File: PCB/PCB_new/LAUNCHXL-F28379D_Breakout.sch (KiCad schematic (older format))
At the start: 21 parts, among them IC1 LM358N, J10 SERVO_CONN, J11 MC_CONN, Q1 220mA/50V/3.5Ω, Q2 100V/17A, Q3 100V/17A, Q4 100V/17A, Q5 100V/17A, Q6 100V/17A

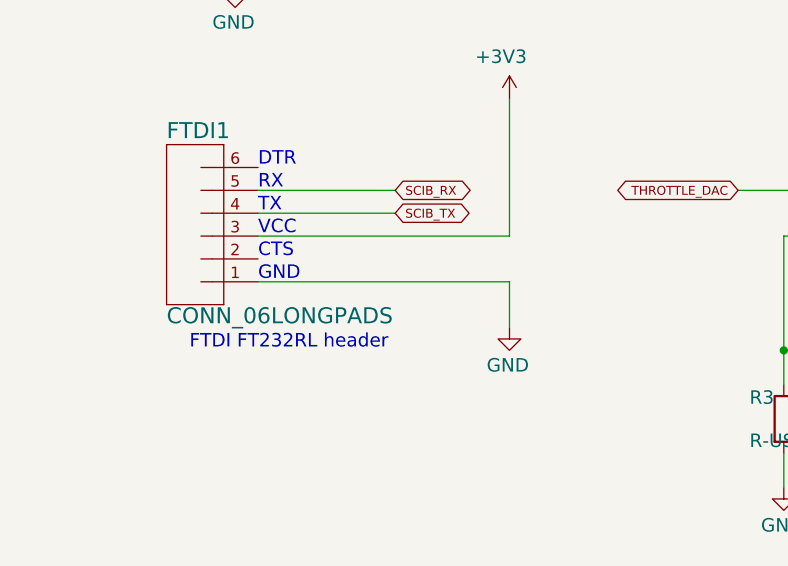
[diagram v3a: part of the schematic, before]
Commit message: changed components footprints to Drivetrain.pretty
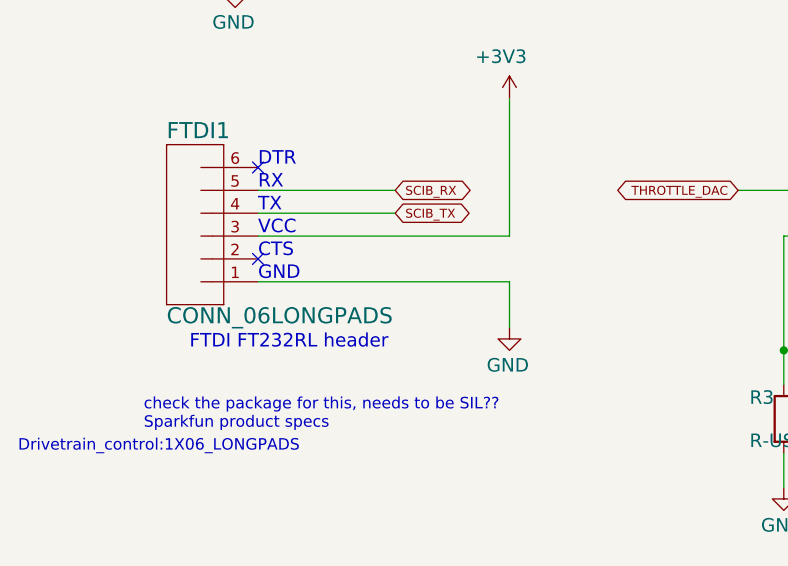
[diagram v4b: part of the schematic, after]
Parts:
- C1: footprint Drivetrain_control:C0805 -> Capacitor_SMD:C_0805_2012Metric_Pad1.15x1.40mm_HandSolder
- DCDC_CONN_12V: footprint Connector_Molex:Molex_CLIK-Mate_502382-0270_1x02-1MP_P1.25mm_Vertical -> Drivetrain_control:22-23-2021
- IC1: footprint Package_DIP:DIP-8_W10.16mm -> Drivetrain_control:DIL08
- J10: footprint (none) -> Drivetrain_control:5566-8
- JETSON_CONN_PWR: footprint Connector_Molex:Molex_CLIK-Mate_502382-0370_1x03-1MP_P1.25mm_Vertical -> Drivetrain_control:22-23-2031
- Q1: footprint Package_TO_SOT_THT:TO-251-3_Vertical -> Drivetrain_control:SOT23-3
- Q2, Q3, Q4, Q5, Q6: footprint Package_TO_SOT_THT:TO-251-3_Vertical -> Drivetrain_control:TO220V
- R1, R18, R2, R3, R4, R5: footprint Drivetrain_control:R0805 -> Resistor_SMD:R_0805_2012Metric_Pad1.15x1.40mm_HandSolder
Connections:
- no-connect marks 0 -> 2
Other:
- note added: "Drivetrain_control:1X06_LONGPADS"
- note added: "check the package for this, needs to be SIL??\nSparkfun product specs"
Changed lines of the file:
@@
 F 0 "R4" V 4600 4200 59  0000 L BNN
 F 1 "R-US_R0805" V 4600 3550 59  0000 L BNN
-F 2 "Drivetrain_control:R0805" H 4700 4100 50  0001 C CNN
+F 2 "Resistor_SMD:R_0805_2012Metric_Pad1.15x1.40mm_HandSolder" H 4700 4100 50  0001 C CNN
 F 3 "" H 4700 4100 50  0001 C CNN
 	1    4700 4100
@@
 F 0 "IC1" H 4750 3625 59  0001 L BNN
 F 1 "LM358N" H 4750 3300 59  0001 L BNN
-F 2 "Package_DIP:DIP-8_W10.16mm" H 4650 3500 50  0001 C CNN
+F 2 "Drivetrain_control:DIL08" H 4650 3500 50  0001 C CNN
 F 3 "" H 4650 3500 50  0001 C CNN
 	1    4650 3500
@@
 F 0 "C1" H 5360 3115 59  0000 L BNN
 F 1 "0.1uF" H 5360 2915 59  0000 L BNN
-F 2 "Drivetrain_control:C0805" H 5300 3100 50  0001 C CNN
+F 2 "Capacitor_SMD:C_0805_2012Metric_Pad1.15x1.40mm_HandSolder" H 5300 3100 50  0001 C CNN
 F 3 "" H 5300 3100 50  0001 C CNN
 	1    5300 3100
@@
 F 0 "Q1" V 5600 1550 70  0000 L BNN
 F 1 "220mA/50V/3.5Ω" V 5700 1350 70  0000 L BNN
-F 2 "Package_TO_SOT_THT:TO-251-3_Vertical" H 5300 1600 50  0001 C CNN
+F 2 "Drivetrain_control:SOT23-3" H 5300 1600 50  0001 C CNN
 F 3 "" H 5300 1600 50  0001 C CNN
 	1    5300 1600
@@
 F 0 "R1" H 4600 1550 59  0000 L BNN
 F 1 "10k" H 4550 1450 59  0000 L BNN
-F 2 "Drivetrain_control:R0805" H 4800 1500 50  0001 C CNN
+F 2 "Resistor_SMD:R_0805_2012Metric_Pad1.15x1.40mm_HandSolder" H 4800 1500 50  0001 C CNN
 F 3 "" H 4800 1500 50  0001 C CNN
 	1    4800 1500
@@
 F 0 "R5" H 6550 2759 59  0000 L BNN
 F 1 "R-US_R0805" H 6550 2570 59  0000 L BNN
-F 2 "Drivetrain_control:R0805" H 6700 2700 50  0001 C CNN
+F 2 "Resistor_SMD:R_0805_2012Metric_Pad1.15x1.40mm_HandSolder" H 6700 2700 50  0001 C CNN
 F 3 "" H 6700 2700 50  0001 C CNN
 	1    6700 2700
@@
 F 0 "Q2" H 7900 3200 70  0000 L BNN
 F 1 "100V/17A" H 7900 3100 70  0000 L BNN
-F 2 "Package_TO_SOT_THT:TO-251-3_Vertical" H 7700 3200 50  0001 C CNN
+F 2 "Drivetrain_control:TO220V" H 7700 3200 50  0001 C CNN
 F 3 "" H 7700 3200 50  0001 C CNN
 	1    7700 3200
@@
 F 0 "R18" H 7650 2759 59  0000 L BNN
 F 1 "R-US_R0805" H 7650 2570 59  0000 L BNN
-F 2 "Drivetrain_control:R0805" H 7800 2700 50  0001 C CNN
+F 2 "Resistor_SMD:R_0805_2012Metric_Pad1.15x1.40mm_HandSolder" H 7800 2700 50  0001 C CNN
 F 3 "" H 7800 2700 50  0001 C CNN
 	1    7800 2700
@@
 F 0 "JETSON_CONN_PWR1" H 9800 1400 51  0000 L BNN
 F 1 "22-23-2031" H 10470 1655 59  0001 L BNN
-F 2 "Connector_Molex:Molex_CLIK-Mate_502382-0370_1x03-1MP_P1.25mm_Vertical" H 10500 1600 50  0001 C CNN
+F 2 "Drivetrain_control:22-23-2031" H 10500 1600 50  0001 C CNN
 F 3 "" H 10500 1600 50  0001 C CNN
 	1    10500 1600
@@
 F 0 "Q3" H 6800 3200 70  0000 L BNN
 F 1 "100V/17A" H 6800 3100 70  0000 L BNN
-F 2 "Package_TO_SOT_THT:TO-251-3_Vertical" H 6600 3200 50  0001 C CNN
+F 2 "Drivetrain_control:TO220V" H 6600 3200 50  0001 C CNN
 F 3 "" H 6600 3200 50  0001 C CNN
 	1    6600 3200
@@
 F 0 "Q4" H 9000 3200 70  0000 L BNN
 F 1 "100V/17A" H 9000 3100 70  0000 L BNN
-F 2 "Package_TO_SOT_THT:TO-251-3_Vertical" H 8800 3200 50  0001 C CNN
+F 2 "Drivetrain_control:TO220V" H 8800 3200 50  0001 C CNN
 F 3 "" H 8800 3200 50  0001 C CNN
 	1    8800 3200
@@
 F 0 "Q5" H 10100 3200 70  0000 L BNN
 F 1 "100V/17A" H 10100 3100 70  0000 L BNN
-F 2 "Package_TO_SOT_THT:TO-251-3_Vertical" H 9900 3200 50  0001 C CNN
+F 2 "Drivetrain_control:TO220V" H 9900 3200 50  0001 C CNN
 F 3 "" H 9900 3200 50  0001 C CNN
 	1    9900 3200
@@
 F 0 "Q6" H 11200 3200 70  0000 L BNN
 F 1 "100V/17A" H 11200 3100 70  0000 L BNN
-F 2 "Package_TO_SOT_THT:TO-251-3_Vertical" H 11000 3200 50  0001 C CNN
+F 2 "Drivetrain_control:TO220V" H 11000 3200 50  0001 C CNN
 F 3 "" H 11000 3200 50  0001 C CNN
 	1    11000 3200
@@
 F 0 "R3" H 4150 4459 59  0000 L BNN
 F 1 "R-US_R0805" H 4150 4270 59  0000 L BNN
-F 2 "Drivetrain_control:R0805" H 4300 4400 50  0001 C CNN
+F 2 "Resistor_SMD:R_0805_2012Metric_Pad1.15x1.40mm_HandSolder" H 4300 4400 50  0001 C CNN
 F 3 "" H 4300 4400 50  0001 C CNN
 	1    4300 4400
@@
 F 0 "R2" H 5600 1500 59  0000 L BNN
 F 1 "10k" H 5550 1400 59  0000 L BNN
-F 2 "Drivetrain_control:R0805" H 5800 1500 50  0001 C CNN
+F 2 "Resistor_SMD:R_0805_2012Metric_Pad1.15x1.40mm_HandSolder" H 5800 1500 50  0001 C CNN
 F 3 "" H 5800 1500 50  0001 C CNN
 	1    5800 1500
@@
 F 0 "DCDC_CONN_12V1" H 6900 1450 51  0000 L BNN
 F 1 "22-23-2021" H 7570 1555 59  0001 L BNN
-F 2 "Connector_Molex:Molex_CLIK-Mate_502382-0270_1x02-1MP_P1.25mm_Vertical" H 7600 1500 50  0001 C CNN
+F 2 "Drivetrain_control:22-23-2021" H 7600 1500 50  0001 C CNN
 F 3 "" H 7600 1500 50  0001 C CNN
 	1    7600 1500
@@
 F 0 "J10" H 3172 1382 50  0000 R CNN
 F 1 "SERVO_CONN" H 3172 1473 50  0000 R CNN
-F 2 "" H 3200 1500 50  0001 C CNN
+F 2 "Drivetrain_control:5566-8" H 3200 1500 50  0001 C CNN
 F 3 "~" H 3200 1500 50  0001 C CNN
 	1    3200 1500
@@
 Wire Wire Line
 	2650 1800 2650 2100
+NoConn ~ 2000 3300
+NoConn ~ 2000 3700
+Text Notes 950  4550 0    50   ~ 0
+Drivetrain_control:1X06_LONGPADS
+Text Notes 1500 4450 0    50   ~ 0
+check the package for this, needs to be SIL??\nSparkfun product specs
 $EndSCHEMATC

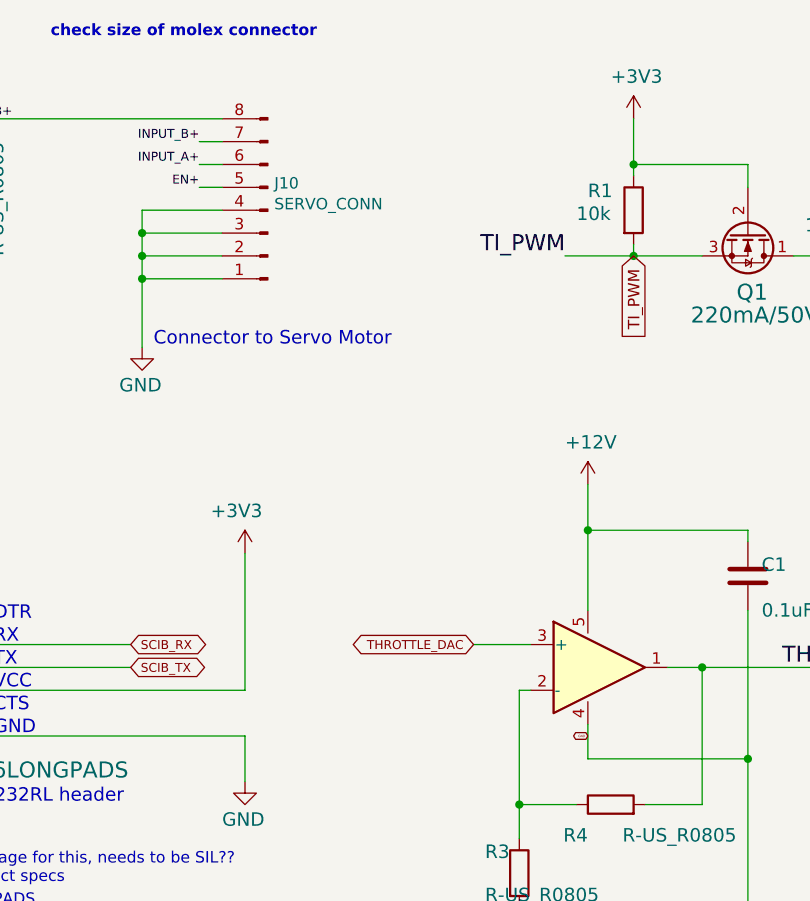
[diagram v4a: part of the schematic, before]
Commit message: tried to update PCB with new components but got weird results (not working)
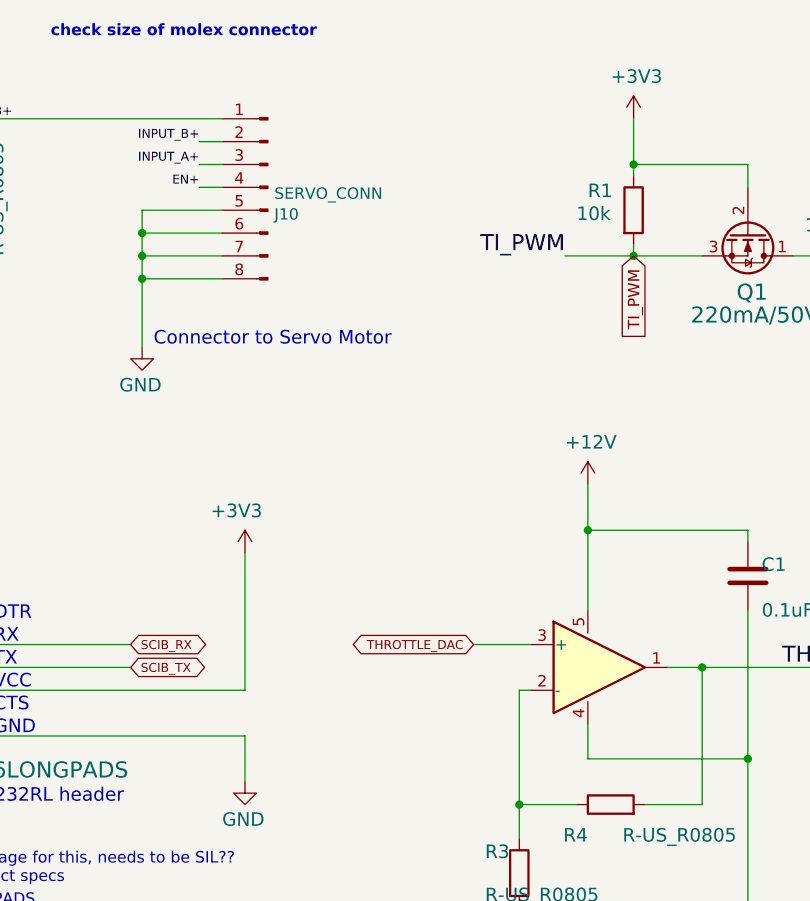
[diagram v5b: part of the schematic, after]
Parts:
- J11: footprint Connector_Molex:Molex_Mini-Fit_Jr_5566-04A2_2x02_P4.20mm_Vertical -> Drivetrain_control:22-23-2041
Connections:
- net EN+: now also J10.4 (Pin_4); no longer J10.5 (Pin_5)
- net GND: now also J10.5 (Pin_5), J10.6 (Pin_6), J10.7 (Pin_7), J10.8 (Pin_8); no longer J10.1 (Pin_1), J10.2 (Pin_2), J10.3 (Pin_3), J10.4 (Pin_4)
- net HLFB+: now also J10.1 (Pin_1); no longer J10.8 (Pin_8)
- net INPUT_A+: now also J10.3 (Pin_3); no longer J10.6 (Pin_6)
- net INPUT_B+: now also J10.2 (Pin_2); no longer J10.7 (Pin_7)
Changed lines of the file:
@@
 	5300 3900 5300 4700
 Connection ~ 5300 3900
-Text GLabel 4600 3800 0    10   BiDi ~ 0
-GND
 Wire Wire Line
 	6700 3400 6700 3500
@@
 Text Notes 2250 750  0    50   ~ 10
 check size of molex connector
-$Comp
-L Connector:Conn_01x08_Male J10
-U 1 1 5DFE807D
-P 3200 1500
-F 0 "J10" H 3172 1382 50  0000 R CNN
-F 1 "SERVO_CONN" H 3172 1473 50  0000 R CNN
-F 2 "Drivetrain_control:5566-8" H 3200 1500 50  0001 C CNN
-F 3 "~" H 3200 1500 50  0001 C CNN
-	1    3200 1500
-	-1   0    0    1
-$EndComp
 Text Notes 2700 2100 0    59   ~ 0
 Connector to Servo Motor
@@
 F 0 "J11" H 11122 4432 50  0000 R CNN
 F 1 "MC_CONN" H 11122 4523 50  0000 R CNN
-F 2 "Connector_Molex:Molex_Mini-Fit_Jr_5566-04A2_2x02_P4.20mm_Vertical" H 11150 4550 50  0001 C CNN
+F 2 "Drivetrain_control:22-23-2041" H 11150 4550 50  0001 C CNN
 F 3 "~" H 11150 4550 50  0001 C CNN
 	1    11150 4550
@@
 Text Notes 1500 4450 0    50   ~ 0
 check the package for this, needs to be SIL??\nSparkfun product specs
+$Comp
+L Connector:Conn_01x08_Male J10
+U 1 1 5DFE807D
+P 3200 1400
+F 0 "J10" H 3172 1282 50  0000 R CNN
+F 1 "SERVO_CONN" H 3172 1373 50  0000 R CNN
+F 2 "Drivetrain_control:5566-8" H 3200 1400 50  0001 C CNN
+F 3 "~" H 3200 1400 50  0001 C CNN
+	1    3200 1400
+	-1   0    0    -1
+$EndComp
 $EndSCHEMATC

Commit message: Created TI schematic and Footprint
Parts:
- Q1: symbol Device:Q_NMOS_DGS -> Device:Q_NMOS_GSD
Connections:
- net +3V3: now also Q1.1 (G); no longer Q1.2 (G)
- net INPUT_B+: now also Q1.3 (D); no longer Q1.1 (D)
- net TI_PWM: now also Q1.2 (S); no longer Q1.3 (S)
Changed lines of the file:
@@
 $EndComp
 $Comp
-L Device:Q_NMOS_DGS Q1
+L Device:Q_NMOS_GSD Q1
 U 1 1 A1BE61D0
 P 5300 1600

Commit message: fixed orientation of the mosfets and other errors in pin layouts
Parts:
- IC1: symbol PCB_2020:LM358_with_power_pins -> PCB_2020:LM358N
- Q2, Q3, Q4, Q5, Q6: symbol Device:Q_NMOS_DGS -> Device:Q_NMOS_GDS
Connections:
- net +12V: now also IC1.8; no longer IC1.5
- net EN+: now also Q3.2 (D); no longer Q3.1 (D)
- net EN+_CTL: now also Q3.1 (G); no longer Q3.2 (G)
- net FS1_CTL: now also Q6.1 (G); no longer Q6.2 (G)
- net FS1_MC: now also Q6.2 (D); no longer Q6.1 (D)
- net FWD_CTL: now also Q5.1 (G); no longer Q5.2 (G)
- net FWD_MC: now also Q5.2 (D); no longer Q5.1 (D)
- net INPUT_A+: now also Q2.2 (D); no longer Q2.1 (D)
- net INPUT_A+_CTL: now also Q2.1 (G); no longer Q2.2 (G)
- net REV_CTL: now also Q4.1 (G); no longer Q4.2 (G)
- net REV_MC: now also Q4.2 (D); no longer Q4.1 (D)
- net THROTTLE_DAC: now also IC1.5 (IN2+); no longer IC1.3 (+)
- net THROTTLE_MC: now also IC1.7 (OUT2); no longer IC1.1
- net at R3.1, R4.1: now also IC1.6 (IN2-); no longer IC1.2 (-)
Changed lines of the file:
@@
 Wire Wire Line
 	10300 1700 10200 1700
-Wire Wire Line
-	5100 3500 5100 4100
-Wire Wire Line
-	5100 3500 5600 3500
 Text Label 5450 3500 0    70   ~ 0
 THROTTLE_MC
@@
 $EndComp
 $Comp
-L PCB_2020:LM358_with_power_pins IC1
+L PCB_2020:LM358N IC1
 U 1 1 70C115B9
-P 4650 3500
+P 4600 3600
 AR Path="/70C115B9" Ref="IC1"  Part="3"
 AR Path="/5DD5E236/70C115B9" Ref="IC1"  Part="3"
 AR Path="/5DF27AC1/70C115B9" Ref="IC1"  Part="1"
-F 0 "IC1" H 4750 3625 59  0001 L BNN
-F 1 "LM358N" H 4750 3300 59  0001 L BNN
-F 2 "Drivetrain_control:DIL08" H 4650 3500 50  0001 C CNN
-F 3 "" H 4650 3500 50  0001 C CNN
-	1    4650 3500
+F 0 "IC1" H 4700 3725 59  0001 L BNN
+F 1 "LM358N" H 4700 3400 59  0001 L BNN
+F 2 "Drivetrain_control:DIL08" H 4600 3600 50  0001 C CNN
+F 3 "" H 4600 3600 50  0001 C CNN
+	1    4600 3600
 	1    0    0    -1
 $EndComp
@@
 $EndComp
 $Comp
-L Device:Q_NMOS_GSD Q1
-U 1 1 A1BE61D0
-P 5300 1600
-AR Path="/A1BE61D0" Ref="Q1"  Part="1"
-AR Path="/5DD5E236/A1BE61D0" Ref="Q1"  Part="1"
-AR Path="/5DF27AC1/A1BE61D0" Ref="Q1"  Part="1"
-F 0 "Q1" V 5600 1550 70  0000 L BNN
-F 1 "220mA/50V/3.5Ω" V 5700 1350 70  0000 L BNN
-F 2 "Drivetrain_control:SOT23-3" H 5300 1600 50  0001 C CNN
-F 3 "" H 5300 1600 50  0001 C CNN
-	1    5300 1600
-	0    1    1    0
-$EndComp
-$Comp
 L Device:R R1
 U 1 1 0B6559E8
@@
 $EndComp
 $Comp
-L Device:Q_NMOS_DGS Q2
+L Device:Q_NMOS_GDS Q2
 U 1 1 BFFF77DC
 P 7700 3200
@@
 INPUT_B+
 $Comp
-L Device:Q_NMOS_DGS Q?
+L Device:Q_NMOS_GDS Q?
 U 1 1 5DF72728
 P 6600 3200
@@
 Connection ~ 6700 3000
 $Comp
-L Device:Q_NMOS_DGS Q?
+L Device:Q_NMOS_GDS Q?
 U 1 1 5DF74B23
 P 8800 3200
@@
 $EndComp
 $Comp
-L Device:Q_NMOS_DGS Q?
+L Device:Q_NMOS_GDS Q?
 U 1 1 5DF76A67
 P 9900 3200
@@
 $EndComp
 $Comp
-L Device:Q_NMOS_DGS Q?
+L Device:Q_NMOS_GDS Q?
 U 1 1 5DF770F2
 P 11000 3200
@@
 	5300 3250 5300 3900
 Wire Wire Line
-	4100 3400 4350 3400
-Wire Wire Line
-	4300 3600 4350 3600
+	4100 3400 4300 3400
 Wire Wire Line
 	4600 3750 4600 3900
 Wire Wire Line
-	4600 2900 4600 3250
-Wire Wire Line
-	4950 3500 5100 3500
-Connection ~ 5100 3500
+	4600 2900 4600 3200
 Wire Wire Line
 	2650 1500 2650 1600
@@
 	-1   0    0    -1
 $EndComp
+$Comp
+L Device:Q_NMOS_GSD Q1
+U 1 1 A1BE61D0
+P 5300 1600
+AR Path="/A1BE61D0" Ref="Q1"  Part="1"
+AR Path="/5DD5E236/A1BE61D0" Ref="Q1"  Part="1"
+AR Path="/5DF27AC1/A1BE61D0" Ref="Q1"  Part="1"
+F 0 "Q1" V 5600 1550 70  0000 L BNN
+F 1 "220mA/50V/3.5Ω" V 5700 1350 70  0000 L BNN
+F 2 "Drivetrain_control:SOT23-3" H 5300 1600 50  0001 C CNN
+F 3 "" H 5300 1600 50  0001 C CNN
+	1    5300 1600
+	0    1    1    0
+$EndComp
+Wire Wire Line
+	5000 3500 5050 3500
+Wire Wire Line
+	5050 3500 5100 3500
+Wire Wire Line
+	5100 3500 5600 3500
+Connection ~ 5100 3500
+Wire Wire Line
+	5100 3500 5100 4100
+Connection ~ 4600 3200
+Wire Wire Line
+	4600 3200 4600 3250
 $EndSCHEMATC

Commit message: new pcb design (still no braking signals)
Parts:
- FTDI: symbol PCB_2020:CONN_06LONGPADS-Drivetrain_control -> Connector:Conn_01x06_Male
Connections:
- net +3V3: now also FTDI.4 (Pin_4); no longer FTDI.3
- net GND: now also FTDI.6 (Pin_6); no longer FTDI.1
- net SCIB_RX: now also FTDI.2 (Pin_2); no longer FTDI.5
- net SCIB_TX: now also FTDI.3 (Pin_3); no longer FTDI.4
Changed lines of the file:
@@
 EESchema Schematic File Version 4
-LIBS:PCB_2020-cache
 EELAYER 30 0
 EELAYER END
@@
 $EndComp
 $Comp
-L PCB_2020:CONN_06LONGPADS-Drivetrain_control FTDI
+L Connector:Conn_01x06_Male FTDI
 U 1 1 A664394C
-P 1800 3600
+P 1800 3500
 AR Path="/A664394C" Ref="FTDI"  Part="1"
 AR Path="/5DD5E236/A664394C" Ref="FTDI"  Part="1"
 AR Path="/5DF27AC1/A664394C" Ref="FTDI1"  Part="1"
-F 0 "FTDI1" H 1600 4020 70  0000 L BNN
-F 1 "CONN_06LONGPADS" H 1600 3210 70  0000 L BNN
-F 2 "Drivetrain_control:1X06_LONGPADS" H 1800 3600 50  0001 C CNN
-F 3 "" H 1800 3600 50  0001 C CNN
-	1    1800 3600
+F 0 "FTDI1" H 1600 3920 70  0000 L BNN
+F 1 "CONN_06LONGPADS" H 1600 3110 70  0000 L BNN
+F 2 "Drivetrain_control:1X06_LONGPADS" H 1800 3500 50  0001 C CNN
+F 3 "" H 1800 3500 50  0001 C CNN
+	1    1800 3500
 	1    0    0    -1
 $EndComp
@@
 Text Notes 10150 900  0    50   ~ 10
 Check to make sure that the mollex connection is correct for these!!
-$Comp
-L Connector:Conn_01x02_Male DCDC_CONN_12V
-U 1 1 F0B3D357
-P 7600 1500
-AR Path="/F0B3D357" Ref="DCDC_CONN_12V"  Part="1"
-AR Path="/5DD5E236/F0B3D357" Ref="DCDC_CONN_12V"  Part="1"
-AR Path="/5DF27AC1/F0B3D357" Ref="DCDC_CONN_12V1"  Part="1"
-F 0 "DCDC_CONN_12V1" H 6900 1450 51  0000 L BNN
-F 1 "22-23-2021" H 7570 1555 59  0001 L BNN
-F 2 "Drivetrain_control:22-23-2021" H 7600 1500 50  0001 C CNN
-F 3 "" H 7600 1500 50  0001 C CNN
-	1    7600 1500
-	-1   0    0    1
-$EndComp
 Text Notes 7700 1150 0    50   ~ 10
 check this mollex connector too!!
@@
 Wire Wire Line
 	4600 3750 4600 3900
-Wire Wire Line
-	4600 2900 4600 3200
 Wire Wire Line
 	2650 1500 2650 1600
@@
 $EndComp
 Wire Wire Line
-	5000 3500 5050 3500
-Wire Wire Line
-	5050 3500 5100 3500
-Wire Wire Line
 	5100 3500 5600 3500
 Connection ~ 5100 3500
 Wire Wire Line
 	5100 3500 5100 4100
-Connection ~ 4600 3200
-Wire Wire Line
-	4600 3200 4600 3250
+Wire Wire Line
+	4600 2900 4600 3250
+Wire Wire Line
+	5000 3500 5100 3500
+$Comp
+L Connector:Conn_01x02_Male DCDC_CONN_12V
+U 1 1 F0B3D357
+P 7600 1500
+AR Path="/F0B3D357" Ref="DCDC_CONN_12V"  Part="1"
+AR Path="/5DD5E236/F0B3D357" Ref="DCDC_CONN_12V"  Part="1"
+AR Path="/5DF27AC1/F0B3D357" Ref="DCDC_CONN_12"  Part="1"
+F 0 "DCDC_CONN_12" H 6900 1450 51  0000 L BNN
+F 1 "22-23-2021" H 7570 1555 59  0001 L BNN
+F 2 "Drivetrain_control:22-23-2021" H 7600 1500 50  0001 C CNN
+F 3 "" H 7600 1500 50  0001 C CNN
+	1    7600 1500
+	-1   0    0    1
+$EndComp
 $EndSCHEMATC
